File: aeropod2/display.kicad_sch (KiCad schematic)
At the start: 1 part, among them J6 Conn_01x07

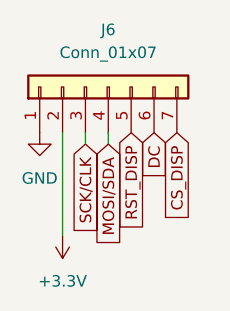
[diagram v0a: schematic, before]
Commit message: Fix schematic faults found in electrical review, add reset/boot buttons
Four faults would have stopped the main board working:

- EN had no pull-up. R4/C5 sat on the unused throw of SW1 while EN was
  left holding only an AC coupled cap, so the module would not have
  booted. R4/C5 now sit on EN, and SW1/SW2 are momentary buttons to
  ground instead of slide switches.
- The microSD was miswired: connections shifted by one pin and CMD tied
  to GND, so no card could ever initialise. The display data line also
  shared a net with the card's DAT0 output. CS now lands on DAT3/CD,
  CMD on IO23 alongside the display, and IO19 is MISO from the card
  alone.
- The boost inductor was never connected to the input rail, so the
  MT3608 had nothing to pump. Rebuilt as VREGIN to L1 to SW plus diode
  anode, with the output caps and feedback divider past the diode.
- The 3.3 V rail had no headroom. R17 is now 100k, putting the boost
  near 5.1 V so the AMS1117 can actually regulate.

Also: backlight control on a new J6 pin 8 driven from IO33, 10k pull-ups
on all five button lines so GPIO35 stops floating, a 100k/100k battery
divider into IO34, both charge LEDs flipped the right way round, 33 ohm
audio series resistors instead of 470, and TP4056 set to about 400 mA.

The CP2102N auto-reset caps are gone. That package brings out RTS but no
DTR, and C30 drove IO0 from CTS, which is an input, so it could not have
worked. Flashing uses the buttons.

Firmware config.h is rewritten against the corrected schematic, and
i2s_output_init now releases the PCM5102A hardware mute on GPIO12, which
nothing was driving.

Schematic passes ERC with no new violations. The PCB has not been
re-laid-out yet, so the main board gerbers are stale; see
ELECTRICAL_REVIEW.md.
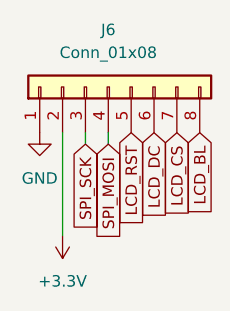
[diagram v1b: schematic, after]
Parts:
- J6: value Conn_01x07 -> Conn_01x08; footprint Connector_PinHeader_2.54mm:PinHeader_1x07_P2.54mm_Vertical -> Connector_PinHeader_2.54mm:PinHeader_1x08_P2.54mm_Vertical; symbol Connector_Generic:Conn_01x07 -> Connector_Generic:Conn_01x08
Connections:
- net CS_DISP renamed LCD_CS
- net DC renamed LCD_DC
- net MOSI/SDA renamed SPI_MOSI
- net RST_DISP renamed LCD_RST
- net SCK/CLK renamed SPI_SCK
- new net LCD_BL: J6.8 (Pin_8)
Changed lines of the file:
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@@
 		)
 	)
-	(global_label "CS_DISP"
+	(global_label "LCD_CS"
 		(shape input)
 		(at 158.75 73.66 270)
@@
 		)
 	)
-	(global_label "RST_DISP"
+	(global_label "LCD_RST"
 		(shape input)
 		(at 153.67 73.66 270)
@@
 		)
 	)
-	(global_label "MOSI/SDA"
+	(global_label "SPI_MOSI"
 		(shape input)
 		(at 151.13 74.93 270)
@@
 		)
 	)
-	(global_label "SCK/CLK"
+	(global_label "SPI_SCK"
 		(shape input)
 		(at 148.59 74.93 270)
@@
 		)
 	)
-	(global_label "DC"
+	(global_label "LCD_DC"
 		(shape input)
 		(at 156.21 73.66 270)
@@
 	)
 	(symbol
-		(lib_id "Connector_Generic:Conn_01x07")
+		(lib_id "Connector_Generic:Conn_01x08")
 		(at 151.13 68.58 90)
 		(unit 1)
@@
 			)
 		)
-		(property "Value" "Conn_01x07"
+		(property "Value" "Conn_01x08"
 			(at 151.13 64.77 90)
 			(show_name no)
@@
 			)
 		)
-		(property "Footprint" "Connector_PinHeader_2.54mm:PinHeader_1x07_P2.54mm_Vertical"
+		(property "Footprint" "Connector_PinHeader_2.54mm:PinHeader_1x08_P2.54mm_Vertical"
 			(at 151.13 68.58 0)
 			(hide yes)
@@
 				)
 			)
+		)
+		(pin "8"
+		)
+	)
+	(global_label "LCD_BL"
+		(shape input)
+		(at 161.29 73.66 270)
+		(effects
+			(font
+				(size 1.27 1.27)
+			)
+			(justify right)
+		)
+		(property "Intersheetrefs" "${INTERSHEET_REFS}"
+			(at 161.29 73.66 0)
+			(hide yes)
+			(show_name no)
+			(do_not_autoplace no)
+			(effects
+				(font
+					(size 1.27 1.27)
+				)
+			)

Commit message: Drop button pull-ups and backlight pin, clear ERC, vendor CP2102N footprint
The five button pull-ups are gone. The only line that actually needed one
was B5, because it sat on GPIO35 and GPIO34-39 are input only with no
internal pull-up. B5 now sits on GPIO33, a full GPIO, so the ESP32's own
pull-ups hold all five buttons high and R20-R24 are removed. GPIO35 is
spare.

The display connector goes back to seven pins. There is no backlight
control line, so the module's BL input is tied to 3.3 V and runs at full
brightness. The LEDC setup is removed and display_backlight() is a no-op
so callers do not change.

The five power_pin_not_driven errors are now properly resolved with
PWR_FLAGs on GND, VBUS, VSYS, AVDD and GNDA. To be clear about the VSS
one: that check looks for a power output pin on each rail and finds none
on a rail fed through a diode, ferrite or net tie. It was never a wiring
fault. Before the fixes it named J5 pin 3 CMD, because CMD was wrongly on
the GND net; afterwards it named J5 pin 6 VSS, which is the card's ground
pin and belongs there. The name moved because CMD left the ground net,
which is what the fix was for. Schematic is now 0 errors, 0 warnings.

The microSD wiring was re-verified pin by pin against the SD spec in SPI
mode: DAT2 and DAT1 unused, CS on DAT3/CD, MOSI on CMD, MISO on DAT0,
CLK on pin 5, VDD on pin 4, VSS on GND. All eight correct.

Footprints for every one of the 67 components were checked against what
is on disk. U6 was pointing at a vendor library in a Downloads folder
via a global nickname, so it built here and nowhere else. That library is
now vendored at aeropod2/footprints.pretty with a project fp-lib-table.

Also gitignores KiCad .lck session files.
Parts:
- J6: value Conn_01x08 -> Conn_01x07; footprint Connector_PinHeader_2.54mm:PinHeader_1x08_P2.54mm_Vertical -> Connector_PinHeader_2.54mm:PinHeader_1x07_P2.54mm_Vertical; symbol Connector_Generic:Conn_01x08 -> Connector_Generic:Conn_01x07
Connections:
- removed net LCD_BL: J6.8 (Pin_8)
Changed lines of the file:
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@@
 	)
 	(symbol
-		(lib_id "Connector_Generic:Conn_01x08")
+		(lib_id "Connector_Generic:Conn_01x07")
 		(at 151.13 68.58 90)
 		(unit 1)
@@
 			)
 		)
-		(property "Value" "Conn_01x08"
+		(property "Value" "Conn_01x07"
 			(at 151.13 64.77 90)
 			(show_name no)
@@
 			)
 		)
-		(property "Footprint" "Connector_PinHeader_2.54mm:PinHeader_1x08_P2.54mm_Vertical"
+		(property "Footprint" "Connector_PinHeader_2.54mm:PinHeader_1x07_P2.54mm_Vertical"
 			(at 151.13 68.58 0)
 			(hide yes)
@@
 				)
 			)
-		)
-		(pin "8"
-		)
-	)
-	(global_label "LCD_BL"
-		(shape input)
-		(at 161.29 73.66 270)
-		(effects
-			(font
-				(size 1.27 1.27)
-			)
-			(justify right)
-		)
-		(property "Intersheetrefs" "${INTERSHEET_REFS}"
-			(at 161.29 73.66 0)
-			(hide yes)
-			(show_name no)
-			(do_not_autoplace no)
-			(effects
-				(font
-					(size 1.27 1.27)
-				)
-			)

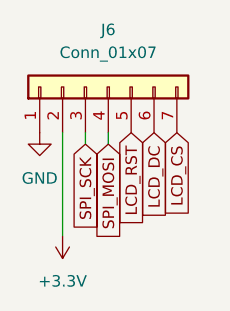
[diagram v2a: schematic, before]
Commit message: Revert schematic, PCB and firmware to the hand-drawn version
Restores aeropod2/*.kicad_sch, aeropod2.kicad_pcb, the firmware pin map
and the BOM to their state at d6429d0, which is byte identical to the
last human-edited revision (2867710). The corrected schematic is still
in history at b35a9fa if any of it is wanted later.

The board file had picked up R18/R19 and the tactile switch footprints
from a schematic update. Nothing hand-made was lost reverting it: track
and via counts were unchanged at 894/147 and the two new parts were
sitting at KiCad's default drop position.

ELECTRICAL_REVIEW.md is rewritten to describe the faults as they stand
in this schematic, and to give the smallest set of layout changes that
makes the board work rather than the full correction.
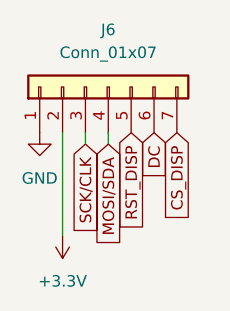
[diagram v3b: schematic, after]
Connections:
- net LCD_CS renamed CS_DISP
- net LCD_DC renamed DC
- net LCD_RST renamed RST_DISP
- net SPI_MOSI renamed MOSI/SDA
- net SPI_SCK renamed SCK/CLK
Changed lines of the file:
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@@
 		)
 	)
-	(global_label "LCD_CS"
+	(global_label "CS_DISP"
 		(shape input)
 		(at 158.75 73.66 270)
@@
 		)
 	)
-	(global_label "LCD_RST"
+	(global_label "RST_DISP"
 		(shape input)
 		(at 153.67 73.66 270)
@@
 		)
 	)
-	(global_label "SPI_MOSI"
+	(global_label "MOSI/SDA"
 		(shape input)
 		(at 151.13 74.93 270)
@@
 		)
 	)
-	(global_label "SPI_SCK"
+	(global_label "SCK/CLK"
 		(shape input)
 		(at 148.59 74.93 270)
@@
 		)
 	)
-	(global_label "LCD_DC"
+	(global_label "DC"
 		(shape input)
 		(at 156.21 73.66 270)
